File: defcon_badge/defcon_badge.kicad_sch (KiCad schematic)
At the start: 0 parts

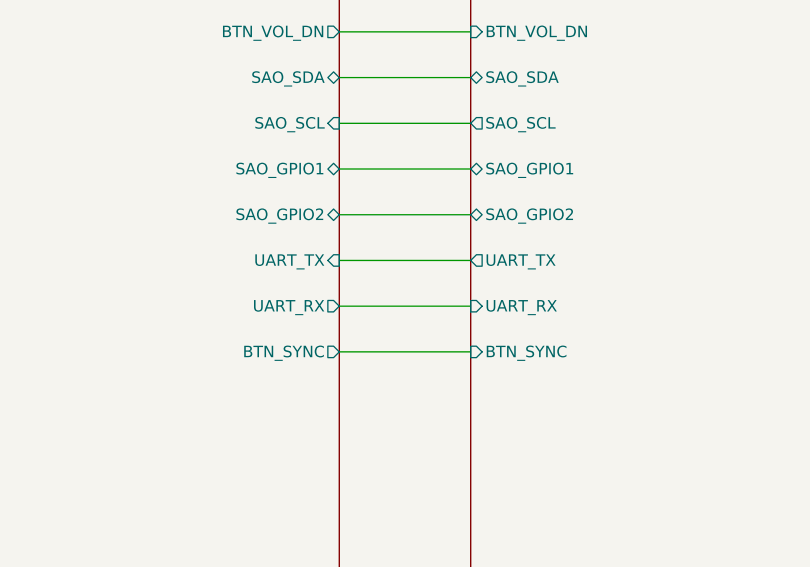
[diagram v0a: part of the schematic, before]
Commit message: Schematic: remove unused J32/J33 debug headers (user request)
The UART debug header (J32, IO sheet) and SWD debug header (J33, MCU_Core)
are unused — the RP2040 is programmed via BOOTSEL/USB (TP1/TP2 pogo pads),
so neither was ever placed on the PCB. Removed both from the schematic so
schematic↔PCB parity stays clean.

Done via a new surgical tool (tools/remove_dev_headers.py) that deletes the
symbols, their power/labels/wires, and the cross-sheet UART plumbing (IO
hier-labels + top-sheet sheet pins + MCU_Core hier-labels/stubs) by
top-level S-expression element, preserving every other symbol UUID (so the
PCB footprint linkage is untouched — no re-sync needed).

The RP2040 debug pins (SWCLK/SWDIO) and UART pins (GP0/GP1) keep their
labels as documented single-pin nets so future test points can attach.

Verified: kicad-cli ERC 0 errors, schematic parity 0 issues. Net warning
delta vs baseline: +4 isolated_pin_label (the intended documented debug
pins), -2 endpoint_off_grid; everything else unchanged.

Co-Authored-By: Claude Opus 4.8 (1M context) <noreply@anthropic.com>
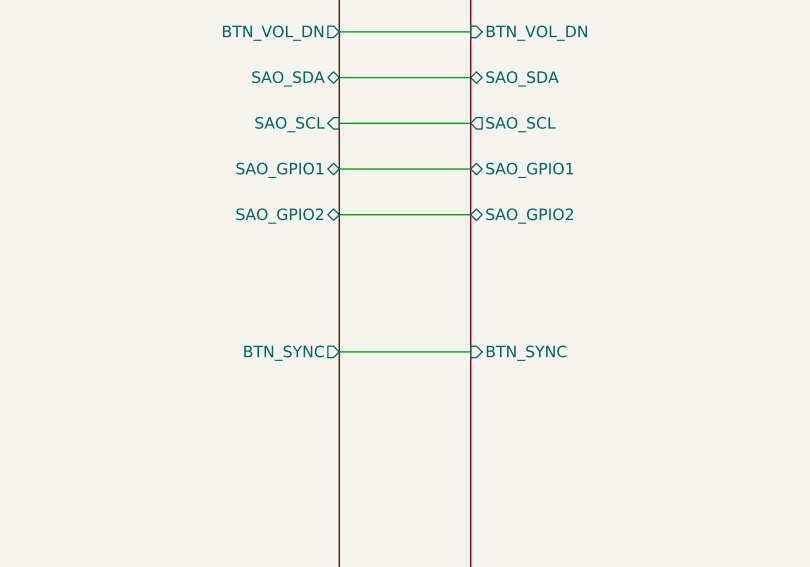
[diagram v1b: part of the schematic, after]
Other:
- sheet IO ports: added none; removed UART_RX, UART_TX
- sheet MCU_Core ports: added none; removed UART_RX, UART_TX
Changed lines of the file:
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@@
-	(wire
-		(pts
-			(xy 150.5 231.14) (xy 165.1 231.14)
-		)
-		(stroke
-			(width 0)
-			(type default)
-		)
-	)
 	(wire
 		(pts
@@
 		(pts
 			(xy 150.5 220.98) (xy 165.1 220.98)
-		)
-		(stroke
-			(width 0)
-			(type default)
-		)
-	)
-	(wire
-		(pts
-			(xy 150.5 226.06) (xy 165.1 226.06)
 		)
 		(stroke
@@
 			)
 		)
-		(pin "UART_TX" input
-			(at 150.5 226.06 0)
-			(effects
-				(font
-					(size 1.27 1.27)
-				)
-				(justify right)
-			)
-		)
-		(pin "UART_RX" output
-			(at 150.5 231.14 0)
-			(effects
-				(font
-					(size 1.27 1.27)
-				)
-				(justify right)
-			)
-		)
 		(pin "BTN_SYNC" output
 			(at 150.5 236.22 0)
@@
 			(effects
 				(font
-					(size 1.27 1.27)
-				)
-				(justify left)
-			)
-		)
-		(pin "UART_TX" output
-			(at 165.1 226.06 180)
-			(effects
-				(font
-					(size 1.27 1.27)
-				)
-				(justify left)
-			)
-		)
-		(pin "UART_RX" input
-			(at 165.1 231.14 180)
-			(effects
-				(font
